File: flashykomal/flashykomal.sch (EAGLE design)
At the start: 29 parts, among them IC1 MEGA8-P, IC2 LM358, IC3 LM2397

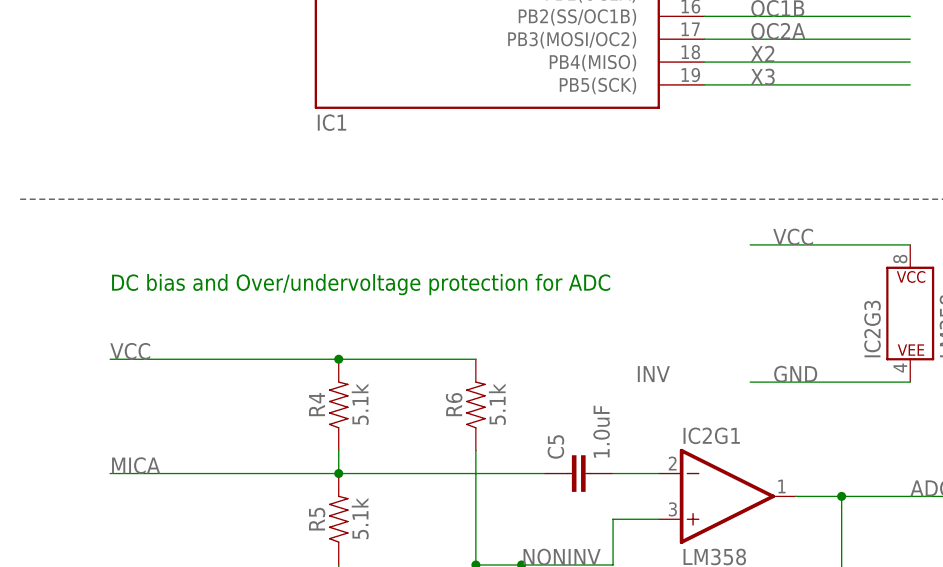
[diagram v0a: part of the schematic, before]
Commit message: Add JP1 markings
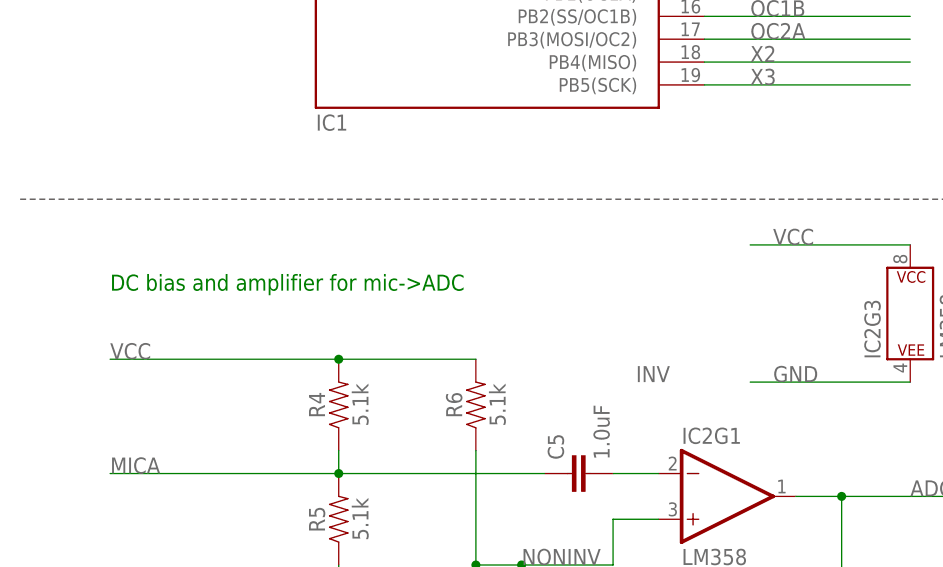
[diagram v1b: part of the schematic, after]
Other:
- note added: "DC bias and amplifier for mic->ADC"
- note removed: "DC bias and Over/undervoltage protection for ADC"
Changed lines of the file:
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@@
 <?xml version="1.0" encoding="utf-8"?>
 <!DOCTYPE eagle SYSTEM "eagle.dtd">
-<eagle version="9.4.2">
+<eagle version="9.1.3">
 <drawing>
 <settings>
@@
 <text x="5.08" y="147.32" size="1.778" layer="91">Separate analog ground plane</text>
 <text x="129.54" y="160.02" size="1.778" layer="91">20 Hz RC filter on switch</text>
-<text x="15.24" y="78.74" size="1.778" layer="91">DC bias and Over/undervoltage protection for ADC</text>
+<text x="15.24" y="78.74" size="1.778" layer="91">DC bias and amplifier for mic-&gt;ADC</text>
 <text x="129.54" y="137.16" size="1.778" layer="91">AVCC filtering</text>
 <text x="12.7" y="43.18" size="1.778" layer="91">MicB</text>

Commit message: Power LED
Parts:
- added D1: (no value), SparkFun-LED:LED0603
- added R15: 330, SparkFun-Resistors:330OHM-0603-1/10W-1%
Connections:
- new net N$1: D1.C, R15.2
- net GND: now also R15.1
- net VCC: now also D1.A, JP4.2
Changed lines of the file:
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@@
 <part name="C7" library="SparkFun-Capacitors" deviceset="10UF-POLAR" device="-RADIAL-2.5MM-25V-20%" value="10uF"/>
 <part name="JP4" library="atmel-samd" deviceset="CONN_03" device=""/>
+<part name="R15" library="SparkFun-Resistors" deviceset="330OHM" device="-0603-1/10W-1%" value="330"/>
+<part name="D1" library="SparkFun-LED" deviceset="LED" device="0603"/>
 </parts>
 <sheets>
@@
 <attribute name="NAME" x="203.2" y="140.208" size="1.778" layer="95" font="vector"/>
 </instance>
+<instance part="R15" gate="G$1" x="246.38" y="160.02" smashed="yes" rot="R90">
+<attribute name="NAME" x="244.856" y="160.02" size="1.778" layer="95" font="vector" rot="R90" align="bottom-center"/>
+<attribute name="VALUE" x="247.904" y="160.02" size="1.778" layer="96" font="vector" rot="R90" align="top-center"/>
+</instance>
+<instance part="D1" gate="G$1" x="246.38" y="170.18"/>
 </instances>
 <busses>
@@
 <label x="241.3" y="154.94" size="1.778" layer="95"/>
 <pinref part="C6" gate="G$1" pin="2"/>
-<wire x1="238.76" y1="154.94" x2="248.92" y2="154.94" width="0.1524" layer="91"/>
+<wire x1="238.76" y1="154.94" x2="246.38" y2="154.94" width="0.1524" layer="91"/>
+<wire x1="246.38" y1="154.94" x2="248.92" y2="154.94" width="0.1524" layer="91"/>
 <wire x1="203.2" y1="144.78" x2="238.76" y2="144.78" width="0.1524" layer="91"/>
 <wire x1="238.76" y1="144.78" x2="238.76" y2="154.94" width="0.1524" layer="91"/>
@@
 <wire x1="203.2" y1="165.1" x2="238.76" y2="165.1" width="0.1524" layer="91"/>
 <wire x1="238.76" y1="165.1" x2="238.76" y2="154.94" width="0.1524" layer="91"/>
+<pinref part="R15" gate="G$1" pin="1"/>
+<junction x="246.38" y="154.94"/>
 </segment>
 <segment>
@@
 <wire x1="203.2" y1="157.48" x2="200.66" y2="157.48" width="0.1524" layer="91"/>
 <junction x="203.2" y="157.48"/>
+</segment>
+<segment>
+<pinref part="JP4" gate="G$1" pin="2"/>
+<wire x1="213.36" y1="134.62" x2="231.14" y2="134.62" width="0.1524" layer="91"/>
+<label x="226.06" y="134.62" size="1.778" layer="95"/>
+</segment>
+<segment>
+<pinref part="D1" gate="G$1" pin="A"/>
+<wire x1="246.38" y1="172.72" x2="231.14" y2="172.72" width="0.1524" layer="91"/>
+<label x="233.68" y="172.72" size="1.778" layer="95"/>
 </segment>
 </net>
@@
 </segment>
 </net>
+<net name="N$1" class="0">
+<segment>
+<pinref part="R15" gate="G$1" pin="2"/>
+<pinref part="D1" gate="G$1" pin="C"/>
+</segment>
+</net>
